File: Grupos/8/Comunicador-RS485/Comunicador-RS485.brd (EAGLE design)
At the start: 70.1 x 59.1 mm, 14 parts, among them P1 10k, T1 SN65HVD3082EDR

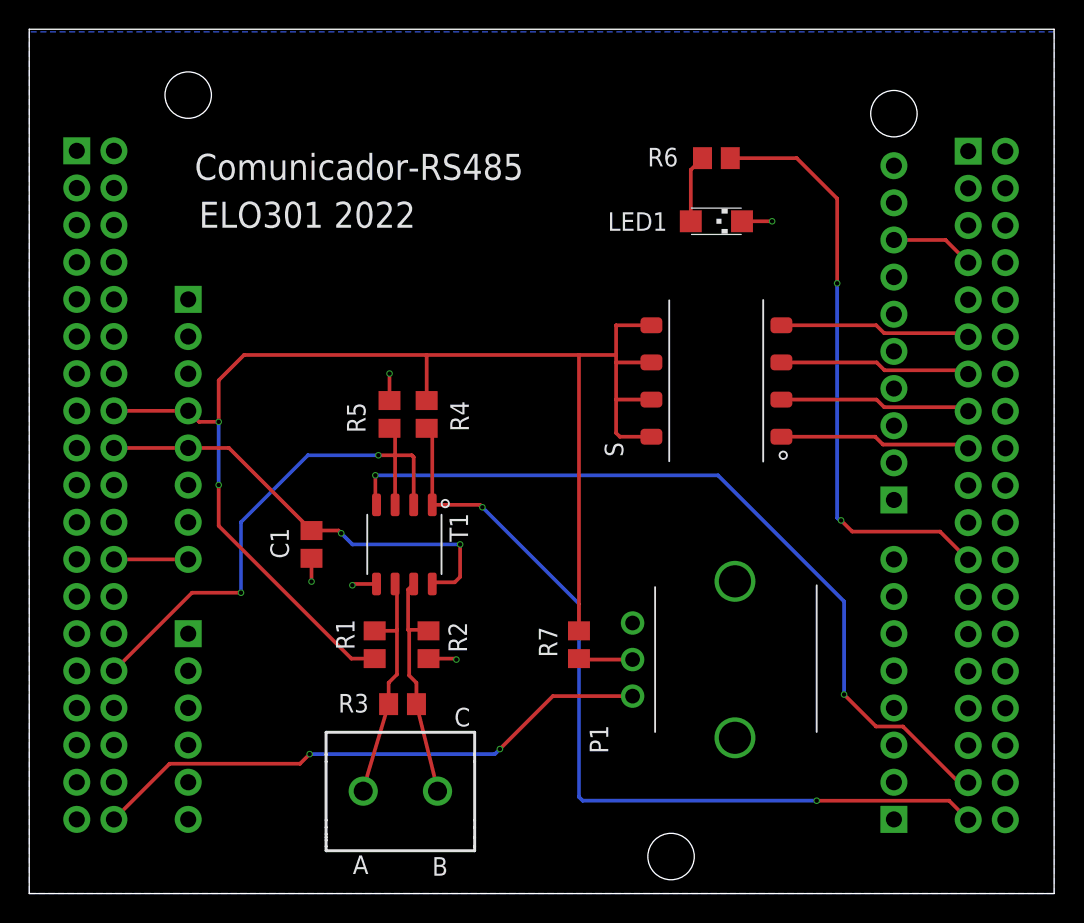
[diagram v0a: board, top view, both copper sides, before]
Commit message: Se mueve el RS485 a UART4
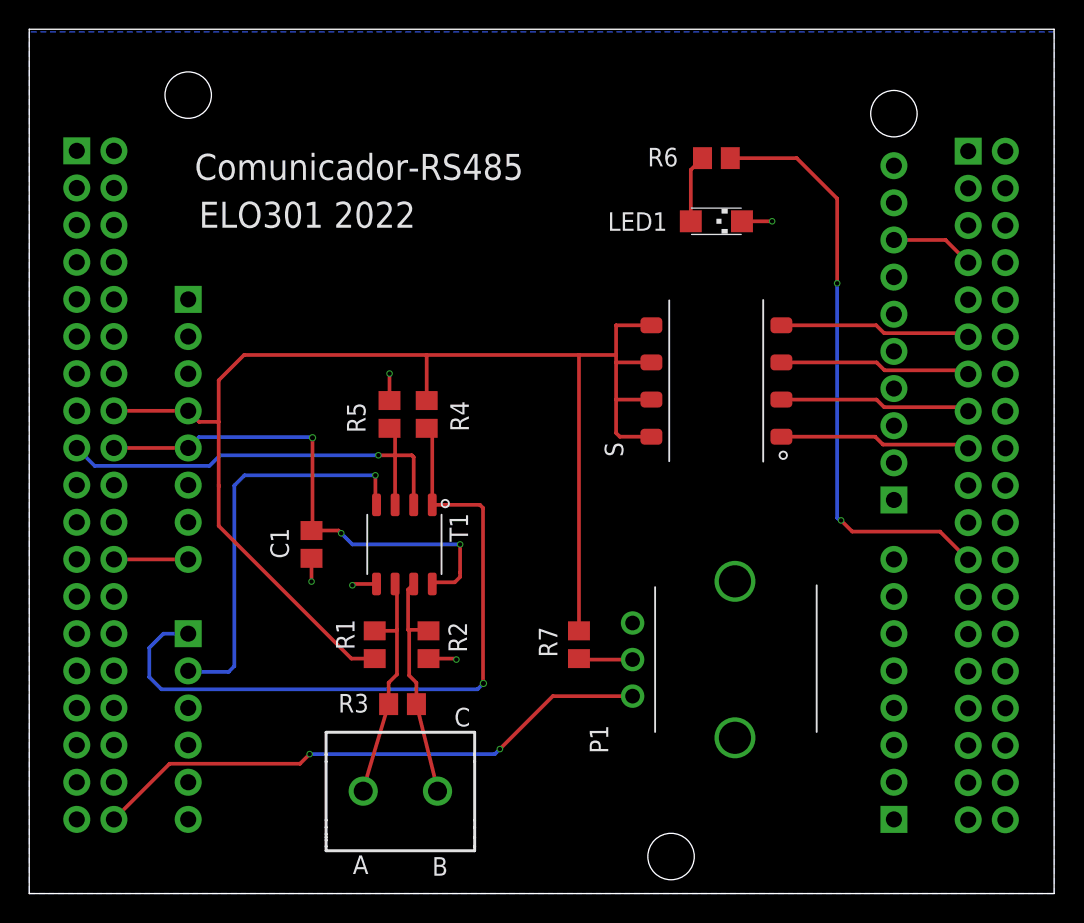
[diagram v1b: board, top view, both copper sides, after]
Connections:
- net DE: now also M1.CN7-17; no longer M1.CN7-30
- net RX: now also M1.CN8-1; no longer M1.CN10-37
- net TX: now also M1.CN8-2; no longer M1.CN10-35
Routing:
- net TX: track 55.0 -> 27.7 mm, vias 2 -> 1
- net RX: track 58.7 -> 49.4 mm, vias 2 -> 1
- net DE: track 38.1 -> 32.6 mm, vias 2 -> 1
- net VCC5V: track 30.7 -> 35.2 mm, vias 2 -> 3
- net VCC: vias 2 -> 0
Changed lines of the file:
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@@
 <drawing>
 <settings>
-<setting alwaysvectorfont="no"/>
+<setting alwaysvectorfont="yes"/>
 <setting verticaltext="up"/>
 </settings>
@@
 <wire x1="51.562" y1="48.768" x2="54.102" y2="48.768" width="0.254" layer="1"/>
 <wire x1="37.592" y1="28.006" x2="36.002" y2="28.006" width="0.254" layer="1"/>
-<wire x1="26.924" y1="37.084" x2="26.924" y2="39.878" width="0.254" layer="1"/>
-<via x="26.924" y="39.878" extent="1-16" drill="0.3"/>
-<wire x1="26.924" y1="39.878" x2="26.924" y2="44.196" width="0.254" layer="16"/>
-<via x="26.924" y="44.196" extent="1-16" drill="0.3"/>
+<wire x1="26.924" y1="37.084" x2="26.924" y2="39.7493" width="0.254" layer="1"/>
+<wire x1="26.924" y1="39.7493" x2="26.924" y2="39.878" width="0.254" layer="1"/>
 <wire x1="26.924" y1="44.196" x2="25.594" y2="44.196" width="0.254" layer="1"/>
 <wire x1="36.002" y1="28.006" x2="26.924" y2="37.084" width="0.254" layer="1"/>
@@
 <wire x1="24.84" y1="44.95" x2="19.76" y2="44.95" width="0.254" layer="1"/>
 <wire x1="25.594" y1="44.196" x2="24.84" y2="44.95" width="0.254" layer="1"/>
+<wire x1="26.924" y1="39.878" x2="26.924" y2="44.196" width="0.254" layer="1"/>
 </signal>
 <signal name="A">
@@
 </signal>
 <signal name="TX">
-<contactref element="M1" pad="CN10-35"/>
 <contactref element="T1" pad="4"/>
 <wire x1="37.719" y1="38.5191" x2="37.639" y2="38.5991" width="0.254" layer="1"/>
 <wire x1="37.639" y1="38.5991" x2="37.639" y2="40.539" width="0.254" layer="1"/>
 <via x="37.639" y="40.539" extent="1-16" drill="0.3"/>
-<wire x1="37.639" y1="40.539" x2="61.07" y2="40.539" width="0.254" layer="16"/>
-<wire x1="61.07" y1="40.539" x2="69.69" y2="31.919" width="0.254" layer="16"/>
-<wire x1="69.69" y1="31.919" x2="69.69" y2="25.55" width="0.254" layer="16"/>
-<via x="69.69" y="25.55" extent="1-16" drill="0.3"/>
-<wire x1="69.69" y1="25.55" x2="71.8759" y2="23.3641" width="0.254" layer="1"/>
-<wire x1="71.8759" y1="23.3641" x2="73.71508125" y2="23.3641" width="0.254" layer="1"/>
-<wire x1="77.554175" y1="19.52500625" x2="78.18" y2="19.52500625" width="0.254" layer="1"/>
-<wire x1="73.71508125" y1="23.3641" x2="77.554175" y2="19.52500625" width="0.254" layer="1"/>
+<contactref element="M1" pad="CN8-2"/>
+<wire x1="37.639" y1="40.539" x2="28.6898" y2="40.539" width="0.254" layer="16"/>
+<wire x1="27.9959" y1="27.4886" x2="27.6079" y2="27.1006" width="0.254" layer="16"/>
+<wire x1="27.6079" y1="27.1006" x2="24.9094" y2="27.1006" width="0.254" layer="16"/>
+<wire x1="24.9094" y1="27.1006" x2="24.84" y2="27.17" width="0.254" layer="16"/>
+<wire x1="28.6898" y1="40.539" x2="27.9959" y2="39.8451" width="0.254" layer="16"/>
+<wire x1="27.9959" y1="39.8451" x2="27.9959" y2="27.4886" width="0.254" layer="16"/>
 </signal>
 <signal name="RX">
-<contactref element="M1" pad="CN10-37"/>
 <contactref element="R4" pad="1"/>
 <contactref element="T1" pad="1"/>
@@
 <wire x1="41.529" y1="43.373" x2="41.148" y2="43.754" width="0.254" layer="1"/>
 <wire x1="41.529" y1="38.5191" x2="44.7929" y2="38.5191" width="0.254" layer="1"/>
-<wire x1="44.7929" y1="38.5191" x2="44.958" y2="38.354" width="0.254" layer="1"/>
-<via x="44.958" y="38.354" extent="1-16" drill="0.3"/>
-<wire x1="44.958" y1="38.354" x2="51.562" y2="31.75" width="0.254" layer="16"/>
-<wire x1="51.562" y1="31.75" x2="51.562" y2="18.542" width="0.254" layer="16"/>
-<wire x1="51.562" y1="18.542" x2="51.816" y2="18.288" width="0.254" layer="16"/>
-<wire x1="51.816" y1="18.288" x2="67.818" y2="18.288" width="0.254" layer="16"/>
-<via x="67.818" y="18.288" extent="1-16" drill="0.3"/>
-<wire x1="67.818" y1="18.288" x2="76.87700625" y2="18.288" width="0.254" layer="1"/>
-<wire x1="76.87700625" y1="18.288" x2="78.18" y2="16.98500625" width="0.254" layer="1"/>
+<contactref element="M1" pad="CN8-1"/>
+<wire x1="24.84" y1="29.71" x2="23.1437" y2="29.71" width="0.254" layer="16"/>
+<wire x1="23.1437" y1="29.71" x2="22.1758" y2="28.7421" width="0.254" layer="16"/>
+<wire x1="22.1758" y1="28.7421" x2="22.1758" y2="26.7424" width="0.254" layer="16"/>
+<wire x1="23.0115" y1="25.9067" x2="22.1758" y2="26.7424" width="0.254" layer="16"/>
+<wire x1="45.0026" y1="26.3104" x2="45.0275" y2="26.3104" width="0.254" layer="1"/>
+<via x="45.0275" y="26.3104" extent="1-16" drill="0.35"/>
+<wire x1="45.0275" y1="26.3104" x2="44.6238" y2="25.9067" width="0.254" layer="16"/>
+<wire x1="44.6238" y1="25.9067" x2="23.0115" y2="25.9067" width="0.254" layer="16"/>
+<wire x1="44.7929" y1="38.5191" x2="45.0026" y2="38.3094" width="0.254" layer="1"/>
+<wire x1="45.0026" y1="38.3094" x2="45.0026" y2="26.3104" width="0.254" layer="1"/>
 </signal>
 <signal name="VCC5V">
 <contactref element="M1" pad="CN6-5"/>
 <contactref element="C1" pad="1"/>
-<wire x1="27.628" y1="42.41" x2="33.274" y2="36.764" width="0.254" layer="1"/>
 <wire x1="33.274" y1="36.764" x2="35.118" y2="36.764" width="0.254" layer="1"/>
 <wire x1="35.118" y1="36.764" x2="35.306" y2="36.576" width="0.254" layer="1"/>
@@
 <contactref element="M1" pad="CN7-18"/>
 <wire x1="24.84" y1="42.41" x2="19.76" y2="42.41" width="0.254" layer="1"/>
-<wire x1="24.84" y1="42.41" x2="27.628" y2="42.41" width="0.254" layer="1"/>
 <contactref element="T1" pad="8"/>
 <wire x1="41.529" y1="33.1089" x2="41.6441" y2="33.224" width="0.254" layer="1"/>
 <wire x1="41.6441" y1="33.224" x2="43.07" y2="33.224" width="0.254" layer="1"/>
 <wire x1="43.07" y1="33.224" x2="43.434" y2="33.588" width="0.254" layer="1"/>
-<wire x1="43.434" y1="33.588" x2="43.434" y2="35.814" width="0.254" layer="1"/>
+<wire x1="43.434" y1="33.588" x2="43.434" y2="33.9056" width="0.254" layer="1"/>
+<wire x1="43.434" y1="33.9056" x2="43.434" y2="35.814" width="0.254" layer="1"/>
+<wire x1="24.84" y1="42.41" x2="25.5796" y2="43.1496" width="0.254" layer="16"/>
+<wire x1="33.3141" y1="43.1496" x2="33.3486" y2="43.1151" width="0.254" layer="16"/>
+<wire x1="33.3486" y1="43.1151" x2="33.34" y2="43.1065" width="0.254" layer="16"/>
+<via x="33.34" y="43.1065" extent="1-16" drill="0.35"/>
+<wire x1="33.34" y1="43.1065" x2="33.34" y2="36.83" width="0.254" layer="1"/>
+<wire x1="33.34" y1="36.83" x2="33.274" y2="36.764" width="0.254" layer="1"/>
+<wire x1="25.5796" y1="43.1496" x2="33.3141" y2="43.1496" width="0.254" layer="16"/>
+<wire x1="43.434" y1="33.9056" x2="43.434" y2="33.9056" width="0.254" layer="1"/>
 </signal>
 <signal name="TIM1">
@@
 </signal>
 <signal name="DE">
-<contactref element="M1" pad="CN7-30"/>
 <contactref element="T1" pad="2"/>
 <contactref element="R5" pad="2"/>
@@
 <wire x1="38.989" y1="41.91" x2="37.846" y2="41.91" width="0.254" layer="1"/>
 <via x="37.846" y="41.91" extent="1-16" drill="0.3"/>
-<wire x1="37.846" y1="41.91" x2="33.02" y2="41.91" width="0.254" layer="16"/>
-<wire x1="28.448" y1="37.338" x2="28.448" y2="32.512" width="0.254" layer="16"/>
-<via x="28.448" y="32.512" extent="1-16" drill="0.3"/>
-<wire x1="28.448" y1="32.512" x2="25.102" y2="32.512" width="0.254" layer="1"/>
-<wire x1="33.02" y1="41.91" x2="28.448" y2="37.338" width="0.254" layer="16"/>
 <wire x1="40.259" y1="41.783" x2="40.132" y2="41.91" width="0.254" layer="1"/>
 <wire x1="40.132" y1="41.91" x2="38.989" y2="41.91" width="0.254" layer="1"/>
 <wire x1="40.259" y1="38.5191" x2="40.259" y2="41.783" width="0.254" layer="1"/>
-<wire x1="25.102" y1="32.512" x2="19.76" y2="27.17" width="0.254" layer="1"/>
+<contactref element="M1" pad="CN7-17"/>
+<wire x1="18.4488" y1="41.1812" x2="17.22" y2="42.41" width="0.254" layer="16"/>
+<wire x1="37.846" y1="41.91" x2="27.0175" y2="41.91" width="0.254" layer="16"/>
+<wire x1="27.0175" y1="41.91" x2="26.2887" y2="41.1812" width="0.254" layer="16"/>
+<wire x1="26.2887" y1="41.1812" x2="18.4488" y2="41.1812" width="0.254" layer="16"/>
 </signal>
 </signals>
